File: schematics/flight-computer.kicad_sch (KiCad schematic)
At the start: 43 parts, among them J1 SWD, J2 BATT, J3 CHG, J4 USB MICRO B, J5 BLACKBOX, U1 STM32F405RGT6, U2 MAX14787E

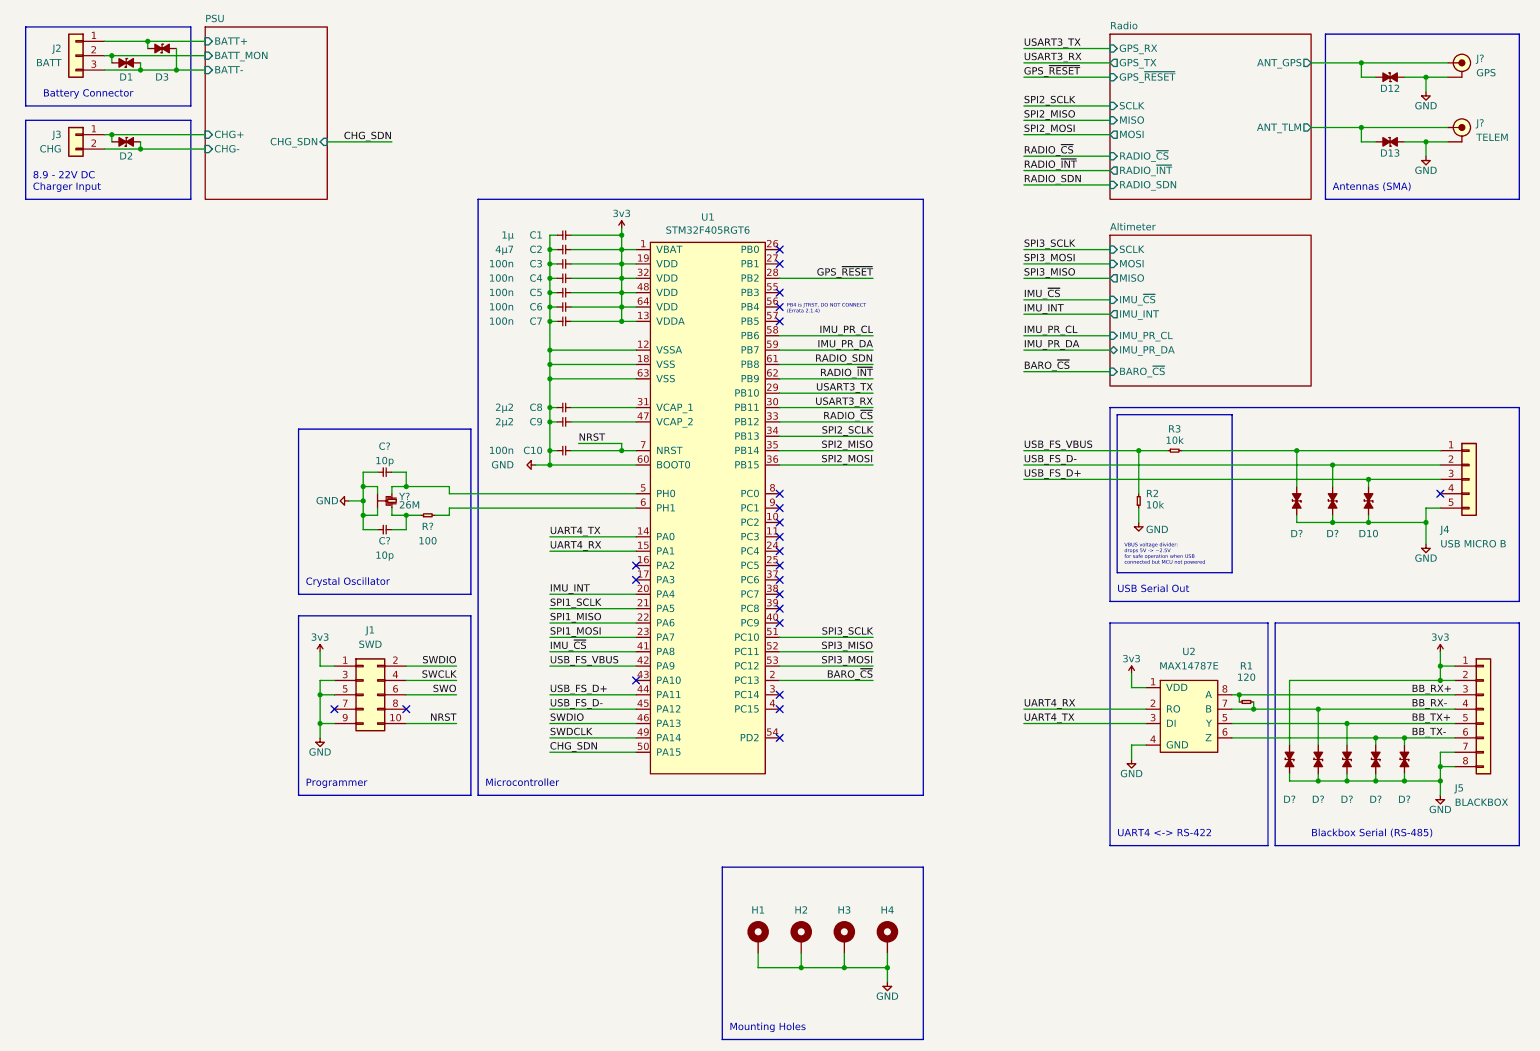
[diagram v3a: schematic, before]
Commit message: Add missing IC footprints
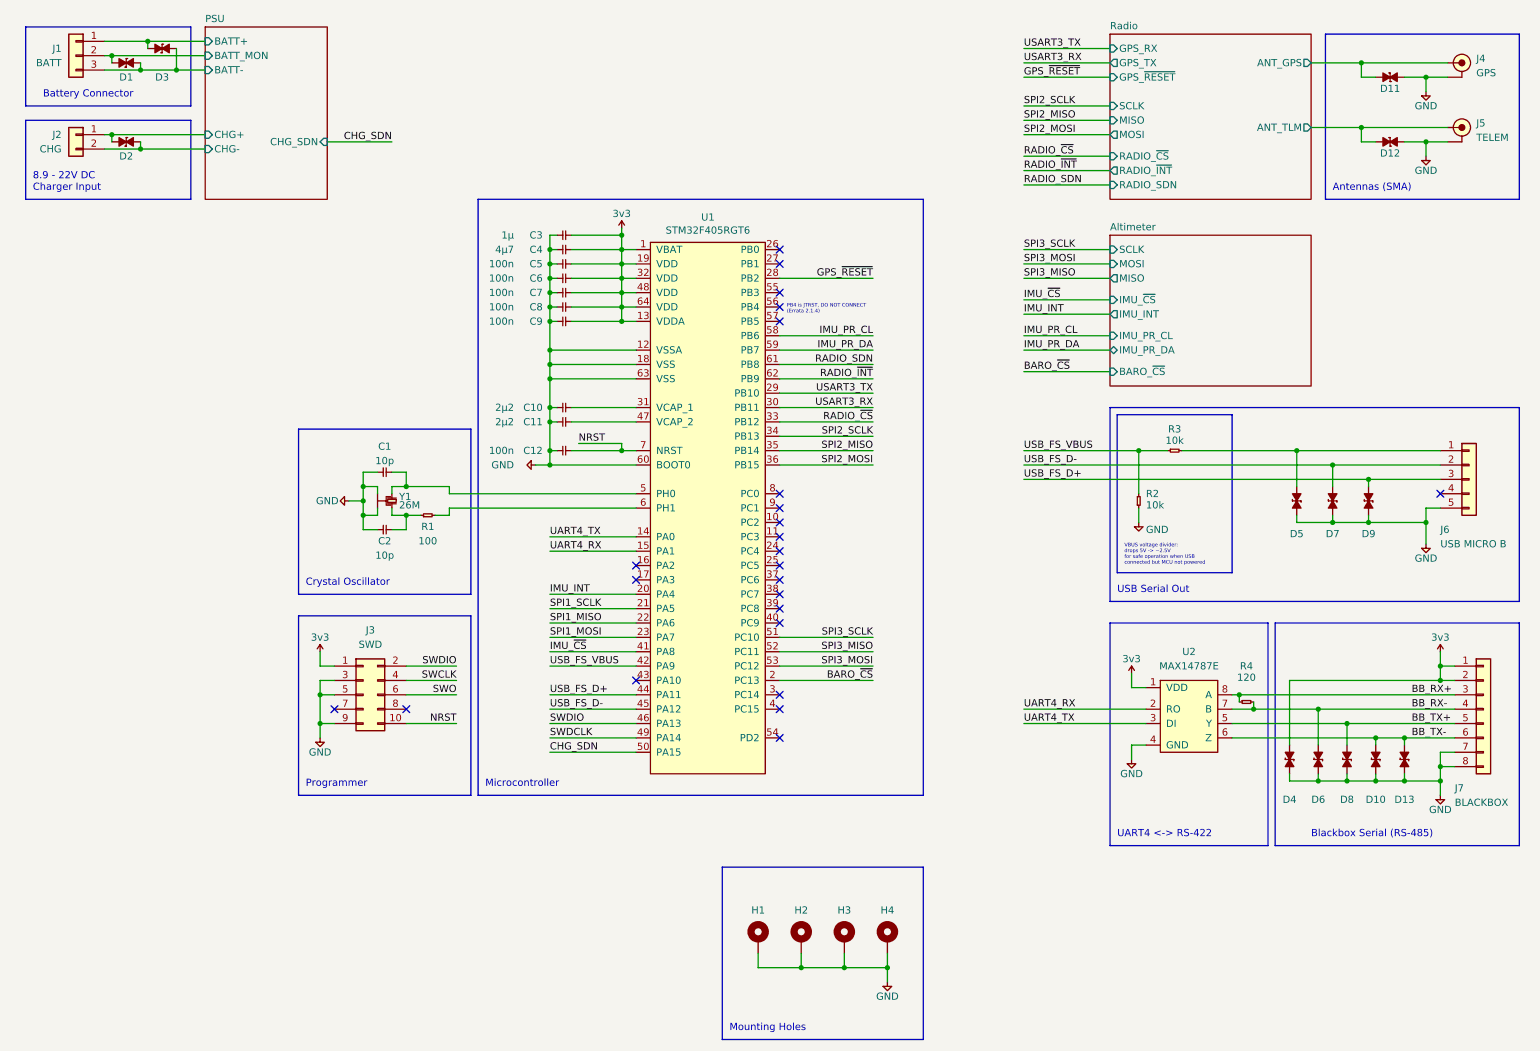
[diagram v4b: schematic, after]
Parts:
- J4, J5: renamed from J?; footprint Strix:SMA-EDGE -> Strix:SMA-Edge
- gave numbers to parts that had none: 11
- renumbered C8 to C10, C9 to C11, C10 to C12, C1 to C3, C2 to C4, C3 to C5, C4 to C6, C5 to C7, C6 to C8, C7 to C9, D12 to D11, D13 to D12, D10 to D9, J2 to J1, J3 to J2, J1 to J3, J4 to J6, J5 to J7, R1 to R4

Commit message: Fix outdated footprint references in symbol lib
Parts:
- J4, J5: footprint Strix:SMA-Edge -> Strix:SMA-EDGE
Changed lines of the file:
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@@
     (pin "1")
   )
-  (symbol (lib_id "Strix:D_ESD") (at 257.81 26.67 0) (unit 1)
+  (symbol (lib_name "D_ESD_8") (lib_id "Strix:D_ESD") (at 257.81 26.67 0) (unit 1)
     (in_bom yes) (on_board yes)
     (property "Reference" "D11" (id 0) (at 257.81 27.94 0)
@@
     (pin "1")
   )
-  (symbol (lib_id "Strix:D_ESD") (at 257.81 38.1 0) (unit 1)
+  (symbol (lib_name "D_ESD_9") (lib_id "Strix:D_ESD") (at 257.81 38.1 0) (unit 1)
     (in_bom yes) (on_board yes)
     (property "Reference" "D12" (id 0) (at 257.81 39.37 0)
@@
     (pin "1")
   )
-  (symbol (lib_id "Strix:D_ESD") (at 255.27 147.32 270) (mirror x) (unit 1)
+  (symbol (lib_name "D_ESD_4") (lib_id "Strix:D_ESD") (at 255.27 147.32 270) (mirror x) (unit 1)
     (in_bom yes) (on_board yes)
     (property "Reference" "D10" (id 0) (at 255.27 153.67 90)
@@
     (pin "2")
   )
-  (symbol (lib_id "Strix:D_ESD") (at 247.65 101.6 270) (mirror x) (unit 1)
+  (symbol (lib_name "D_ESD_7") (lib_id "Strix:D_ESD") (at 247.65 101.6 270) (mirror x) (unit 1)
     (in_bom yes) (on_board yes)
     (property "Reference" "D7" (id 0) (at 247.65 106.68 90)
@@
       (effects (font (size 1.27 1.27)) (justify left))
     )
-    (property "Footprint" "Strix:SMA-Edge" (id 2) (at 270.51 29.464 0)
+    (property "Footprint" "Strix:SMA-EDGE" (id 2) (at 270.51 29.464 0)
       (effects (font (size 1.27 1.27)) hide)
     )
@@
     (pin "1")
   )
-  (symbol (lib_id "Strix:D_ESD") (at 260.35 147.32 270) (mirror x) (unit 1)
+  (symbol (lib_name "D_ESD_5") (lib_id "Strix:D_ESD") (at 260.35 147.32 270) (mirror x) (unit 1)
     (in_bom yes) (on_board yes)
     (property "Reference" "D13" (id 0) (at 260.35 153.67 90)
@@
     (pin "4")
   )
-  (symbol (lib_id "Strix:D_ESD") (at 34.29 24.13 0) (mirror x) (unit 1)
+  (symbol (lib_name "D_ESD_1") (lib_id "Strix:D_ESD") (at 34.29 24.13 0) (mirror x) (unit 1)
     (in_bom yes) (on_board yes)
     (property "Reference" "D1" (id 0) (at 34.29 26.67 0))
@@
       (effects (font (size 1.27 1.27)) (justify left))
     )
-    (property "Footprint" "Strix:SMA-Edge" (id 2) (at 270.51 40.894 0)
+    (property "Footprint" "Strix:SMA-EDGE" (id 2) (at 270.51 40.894 0)
       (effects (font (size 1.27 1.27)) hide)
     )
@@
     (pin "2")
   )
-  (symbol (lib_id "Strix:D_ESD") (at 40.64 21.59 0) (mirror x) (unit 1)
+  (symbol (lib_name "D_ESD_2") (lib_id "Strix:D_ESD") (at 40.64 21.59 0) (mirror x) (unit 1)
     (in_bom yes) (on_board yes)
     (property "Reference" "D3" (id 0) (at 40.64 26.67 0))
@@
     (pin "2")
   )
-  (symbol (lib_id "Strix:D_ESD") (at 245.11 147.32 270) (mirror x) (unit 1)
+  (symbol (lib_name "D_ESD_12") (lib_id "Strix:D_ESD") (at 245.11 147.32 270) (mirror x) (unit 1)
     (in_bom yes) (on_board yes)
     (property "Reference" "D6" (id 0) (at 245.11 153.67 90)
@@
     (pin "2")
   )
-  (symbol (lib_id "Strix:D_ESD") (at 254 101.6 270) (mirror x) (unit 1)
+  (symbol (lib_name "D_ESD_6") (lib_id "Strix:D_ESD") (at 254 101.6 270) (mirror x) (unit 1)
     (in_bom yes) (on_board yes)
     (property "Reference" "D9" (id 0) (at 254 106.68 90)
@@
     (pin "2")
   )
-  (symbol (lib_id "Strix:D_ESD") (at 250.19 147.32 270) (mirror x) (unit 1)
+  (symbol (lib_name "D_ESD_11") (lib_id "Strix:D_ESD") (at 250.19 147.32 270) (mirror x) (unit 1)
     (in_bom yes) (on_board yes)
     (property "Reference" "D8" (id 0) (at 250.19 153.67 90)
@@
     (pin "2")
   )
-  (symbol (lib_id "Strix:D_ESD") (at 34.29 38.1 0) (mirror x) (unit 1)
+  (symbol (lib_name "D_ESD_3") (lib_id "Strix:D_ESD") (at 34.29 38.1 0) (mirror x) (unit 1)
     (in_bom yes) (on_board yes)
     (property "Reference" "D2" (id 0) (at 34.29 40.64 0))
@@
     (pin "9")
   )
-  (symbol (lib_id "Strix:D_ESD") (at 241.3 101.6 270) (mirror x) (unit 1)
+  (symbol (lib_name "D_ESD_10") (lib_id "Strix:D_ESD") (at 241.3 101.6 270) (mirror x) (unit 1)
     (in_bom yes) (on_board yes)
     (property "Reference" "D5" (id 0) (at 241.3 106.68 90)
@@
     )
     (path "/9f5b92df-a9fc-40a8-958b-14377f29c85a"
-      (reference "D1") (unit 1) (value "D_ESD") (footprint "cusf:D_0402")
+      (reference "D1") (unit 1) (value "D_ESD") (footprint "Strix:D_0402")
     )
     (path "/e26e50c4-cf70-4f87-928a-0e6d36a91c09"
-      (reference "D2") (unit 1) (value "D_ESD") (footprint "cusf:D_0402")
+      (reference "D2") (unit 1) (value "D_ESD") (footprint "Strix:D_0402")
     )
     (path "/c3b69905-b979-4ca9-8e95-d758dcfb4921"
-      (reference "D3") (unit 1) (value "D_ESD") (footprint "cusf:D_0402")
+      (reference "D3") (unit 1) (value "D_ESD") (footprint "Strix:D_0402")
     )
     (path "/897d8e03-cc99-497d-94e1-07c9a72484e0"
-      (reference "D4") (unit 1) (value "D_ESD") (footprint "cusf:D_0402")
+      (reference "D4") (unit 1) (value "D_ESD") (footprint "Strix:D_0402")
     )
     (path "/ed524139-d90d-40e9-94d4-80bbe1243464"
-      (reference "D5") (unit 1) (value "D_ESD") (footprint "cusf:D_0402")
+      (reference "D5") (unit 1) (value "D_ESD") (footprint "Strix:D_0402")
     )
     (path "/c53f9a1a-813c-4324-b221-cedf75304ce7"
-      (reference "D6") (unit 1) (value "D_ESD") (footprint "cusf:D_0402")
+      (reference "D6") (unit 1) (value "D_ESD") (footprint "Strix:D_0402")
     )
     (path "/2ac89f34-2885-441c-8a07-6d3539cc8270"
-      (reference "D7") (unit 1) (value "D_ESD") (footprint "cusf:D_0402")
+      (reference "D7") (unit 1) (value "D_ESD") (footprint "Strix:D_0402")
     )
     (path "/de5a4ede-b270-453a-b488-596030c813d8"
-      (reference "D8") (unit 1) (value "D_ESD") (footprint "cusf:D_0402")
+      (reference "D8") (unit 1) (value "D_ESD") (footprint "Strix:D_0402")
     )
     (path "/d36269cf-fe8c-4740-ac3a-02fa7488e4e2"
-      (reference "D9") (unit 1) (value "D_ESD") (footprint "cusf:D_0402")
+      (reference "D9") (unit 1) (value "D_ESD") (footprint "Strix:D_0402")
     )
     (path "/13916f25-a64a-411b-bcf0-66cd269ab1d5"
-      (reference "D10") (unit 1) (value "D_ESD") (footprint "cusf:D_0402")
+      (reference "D10") (unit 1) (value "D_ESD") (footprint "Strix:D_0402")
     )
     (path "/00000000-0000-0000-0000-000060d1b9af"
-      (reference "D11") (unit 1) (value "D_ESD") (footprint "cusf:D_0402")
+      (reference "D11") (unit 1) (value "D_ESD") (footprint "Strix:D_0402")
     )
     (path "/00000000-0000-0000-0000-000060d652b8"
-      (reference "D12") (unit 1) (value "D_ESD") (footprint "cusf:D_0402")
+      (reference "D12") (unit 1) (value "D_ESD") (footprint "Strix:D_0402")
     )
     (path "/696527dd-3c5b-4dc5-bb82-f499fd6dca2d"
-      (reference "D13") (unit 1) (value "D_ESD") (footprint "cusf:D_0402")
+      (reference "D13") (unit 1) (value "D_ESD") (footprint "Strix:D_0402")
     )
     (path "/0560d9e6-7a86-479d-84fc-0ec915d62cea/6d89a26b-fadc-4d42-8ad7-831c9a1bef6d"
@@
     )
     (path "/00000000-0000-0000-0000-0000619fd90a/d6a46229-9234-4b62-ad95-881eeaba2e81"
-      (reference "U4") (unit 1) (value "PCA9306") (footprint "")
+      (reference "U4") (unit 1) (value "PCA9306") (footprint "Strix:PCA9306")
     )
     (path "/00000000-0000-0000-0000-0000619fd90a/833dc3ca-5f5d-42c4-8e71-f9478a5a71c3"

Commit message: Preliminary board layout
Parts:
- removed D13: D_ESD, cusf:D_0402, symbol Strix:D_ESD
- removed J6: USB MICRO B, symbol Strix:Conn_01x05
- removed J7: BLACKBOX, Strix:Molex_Nano-Fit_105314-1108, symbol Strix:Conn_01x08
- removed R2: 10k, Strix:R_0402, symbol Strix:R
- added D11, D12: D_ESD, Strix:D_0402, symbol Strix:D_ESD
- added J4: BLACKBOX, Strix:Molex_Nano-Fit_105314-1108, symbol Strix:Conn_02x04
- added J5: USB C, Strix:USB_C, symbol Strix:USB_C
- added J9: Expansion Slot, Strix:Header_RaspberryPi, symbol Strix:Conn_02x20
- added R4: 10k, Strix:R_0402, symbol Strix:R
- D1, D10, D2, D3, D4, D5, D6, D7, D8, D9: footprint cusf:D_0402 -> Strix:D_0402
- D13: renamed from D11; footprint cusf:D_0402 -> Strix:D_0402
- D14: renamed from D12; footprint cusf:D_0402 -> Strix:D_0402
- J2: footprint (none) -> Strix:Molex_Nano-Fit_105313-1102
- J3: footprint (none) -> Strix:Header_SWD
- J6: renamed from J4; footprint Strix:SMA-EDGE -> Strix:SMA-Edge
- J7: renamed from J5; footprint Strix:SMA-EDGE -> Strix:SMA-Edge
- renumbered R4 to R1, R1 to R2, U2 to U1, U1 to U2
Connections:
- net 3v3: now also D6.2, D7.2, J4.1 (Pin_1), J4.2 (Pin_2); no longer D4.2
- net BB_RX+: now also D5.2, J4.3 (Pin_3)
- net BB_RX-: now also D8.2, J4.4 (Pin_4); no longer D6.2
- net BB_TX+: now also D4.2, J4.5 (Pin_5); no longer D8.2
- net BB_TX-: now also D9.2, J4.6 (Pin_6); no longer D10.2
- net GND: now also R3.1, D11.1, D12.1, J4.7 (Pin_7), J4.8 (Pin_8), J5.A1 (GND), J5.A12 (GND), J5.B1 (GND), J5.B12 (GND), J5.S1 (SHIELD)
- net USB_FS_D+: now also D12.2, J5.A6 (D+), J5.B6 (D+); no longer D9.2
- net USB_FS_D-: now also D11.2, J5.A7 (D-), J5.B7 (D-); no longer D7.2
- net USB_FS_VBUS: now also R3.2, R4.1; no longer R3.1
- new net: D10.2, J5.A4 (VBUS), J5.A9 (VBUS), J5.B4 (VBUS), J5.B9 (VBUS), R4.2
- no-connect marks 24 -> 27
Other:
- moved on the sheet: R1, U1

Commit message: Rough power and RF layouts
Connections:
- net 3v3: now also J9.1 (Pin_1), J9.17 (Pin_17)
- net BB_RX+: now also D8.2, J4.4 (Pin_4); no longer D5.2, J4.3 (Pin_3)
- net BB_RX-: now also D5.2, J4.3 (Pin_3); no longer D8.2, J4.4 (Pin_4)
- net BB_TX+: now also D9.2, J4.6 (Pin_6); no longer D4.2, J4.5 (Pin_5)
- net BB_TX-: now also D4.2, J4.5 (Pin_5); no longer D9.2, J4.6 (Pin_6)
- net GND: now also J9.14 (Pin_14), J9.20 (Pin_20), J9.25 (Pin_25), J9.30 (Pin_30), J9.34 (Pin_34), J9.39 (Pin_39), J9.6 (Pin_6), J9.9 (Pin_9)
- net EXT_RX: now reaches J9.10 (Pin_10)
- net EXT_MOSI: now reaches J9.19 (Pin_19)
- net EXT_MISO: now reaches J9.21 (Pin_21)
- net EXT_SCLK: now reaches J9.23 (Pin_23)
- net EXT_SDA: now reaches J9.3 (Pin_3)
- net EXT_SCL: now reaches J9.5 (Pin_5)
- net EXT_TX: now reaches J9.8 (Pin_8)
- no-connect marks 27 -> 35
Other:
- note added: "Raspberry Pi 'Compatible' Connector"
- moved on the sheet: C1, C10, C11, C12, C2, C3, C4, C5, C6, C7, C8, C9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
